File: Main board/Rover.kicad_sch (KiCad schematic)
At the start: 11 parts, among them J1 IN, J2 OUT, J3 Barrel_Jack_Switch, J4 MOTOR, J5 MOTOR, J6 MOTOR, J7 MOTOR, SW1 SW_DPDT_x2, U1 RASPBERRY_PI_4B_4GB

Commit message: updated pcb
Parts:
- removed U1: RASPBERRY_PI_4B_4GB, RASPBERRY_PI_4B_4GB:MODULE_RASPBERRY_PI_4B_4GB, symbol RASPBERRY_PI_4B_4GB:RASPBERRY_PI_4B_4GB
- added D1: LED, LED_THT:LED_D5.0mm_Clear, symbol Device:LED
- added J8: IMU, Connector_PinHeader_2.54mm:PinHeader_1x08_P2.54mm_Vertical, symbol Connector:Conn_01x04_Pin
- added U1: ESP32-DEVKITC-32D, Library:MODULE_ESP32-DEVKITC-32D, symbol ESP32-DEVKITC-32D:ESP32-DEVKITC-32D
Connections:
- net +5V: now also J8.1 (Pin_1), U1.J2-19 (EXT_5V)
- net GND: now also D1.1 (K), J8.2 (Pin_2), U1.J3-1 (GND3)
- net SIG A 1: now also U1.J2-6 (IO35)
- net SIG A 2: now also U1.J2-4 (SENSOR_VN)
- net SIG A 3: now also U1.J3-5 (RXD0)
- net SIG A 4: now also U1.J3-15 (IO2)
- net SIG B 1: now also U1.J2-5 (IO34)
- net SIG B 2: now also U1.J2-3 (SENSOR_VP)
- net SIG B 3: now also U1.J3-4 (TXD0)
- net SIG B 4: now also U1.J3-14 (IO0)
- net IN1 1: no longer names the net of U2.2 (IN1)
- net IN1 1: now also U1.J2-8 (IO33)
- net IN1 2: no longer names the net of U3.2 (IN1)
- net IN1 2: now also U1.J3-9 (IO18)
- net IN2 1: no longer names the net of U2.3 (IN2)
- net IN2 1: now also U1.J2-9 (IO25)
- net IN2 2: no longer names the net of U3.3 (IN2)
- net IN2 2: now also U1.J3-10 (IO5)
- net IN3 1: no longer names the net of U2.4 (IN3)
- net IN3 1: now also U1.J2-10 (IO26)
- net IN3 2: no longer names the net of U3.4 (IN3)
- net IN3 2: now also U1.J3-11 (IO17)
- net IN4 1: no longer names the net of U2.5 (IN4)
- net IN4 1: now also U1.J2-11 (IO27)
- net IN4 2: no longer names the net of U3.5 (IN4)
- net IN4 2: now also U1.J3-12 (IO16)
- net PWM0: no longer names the net of U3.1 (ENA)
- net PWM0: now also U1.J3-8 (IO19)
- net PWM1: no longer names the net of U2.1 (ENA)
- net PWM1: now also U1.J2-7 (IO32)
- net PWM2: no longer names the net of U3.6 (ENB)
- net PWM2: now also U1.J3-13 (IO4)
- net PWM3: no longer names the net of U2.6 (ENB)
- net PWM3: now also U1.J2-12 (IO14)
- new net: J8.3 (Pin_3), U1.J3-3 (IO22)
- new net: J8.4 (Pin_4), U1.J3-6 (IO21)
- new net: D1.2 (A), U1.J3-16 (IO15)
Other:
- note added: "6V MOTOR GND ENCODER GND ENCODER VCC SIG A SIG B"
- moved on the sheet: J1, J2, J3, J4, J5, J6, J7, SW1A, U2, U3

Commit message: message
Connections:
- net at J8.3 (Pin_3): no longer U1.J3-3 (IO22)
- net at J8.4 (Pin_4): no longer U1.J3-6 (IO21)
- net MOTOR_4_DIR_FORWARD: now reaches U2.4 (IN3)
- net MOTOR_4_DIR_FORWARD: now also U1.J3-13 (IO4); no longer U1.J2-10 (IO26)
- net MOTOR_1_DIR_FORWARD: now reaches U1.J2-11 (IO27)
- net MOTOR_1_DIR_FORWARD: now also U3.2 (IN1); no longer U2.5 (IN4)
- net MOTOR_1_DIR_REVERSE: now reaches U1.J2-12 (IO14)
- net MOTOR_1_DIR_REVERSE: now also U3.3 (IN2); no longer U2.6 (ENB)
- net MOTOR_2_DIR_FORWARD: now reaches U1.J2-13 (IO12)
- net MOTOR_2_DIR_FORWARD: now also U3.4 (IN3)
- net MOTOR_2_DIR_REVERSE: now reaches U1.J2-15 (IO13)
- net MOTOR_2_DIR_REVERSE: now also U3.5 (IN4)
- net MOTOR_1_PWM: now reaches U1.J2-7 (IO32)
- net MOTOR_1_PWM: now also U3.1 (ENA); no longer U2.1 (ENA)
- net MOTOR_2_PWM: now reaches U1.J2-8 (IO33)
- net MOTOR_2_PWM: now also U3.6 (ENB); no longer U2.2 (IN1)
- net MOTOR_3_DIR_REVERSE: now reaches U2.3 (IN2)
- net MOTOR_3_DIR_REVERSE: now also U1.J3-12 (IO16); no longer U1.J2-9 (IO25)
- net MOTOR_4_ENCODER_B: now reaches U1.J3-10 (IO5)
- net MOTOR_4_ENCODER_B: now also J5.6 (Pin_6); no longer U3.3 (IN2)
- net MOTOR_3_DIR_FORWARD: now reaches U1.J3-11 (IO17)
- net MOTOR_3_DIR_FORWARD: now also U2.2 (IN1); no longer U3.4 (IN3)
- net MOTOR_1_ENCODER_A: now reaches U1.J3-2 (IO23)
- net MOTOR_1_ENCODER_A: now also J6.5 (Pin_5)
- net MOTOR_3_ENCODER_B: now reaches U1.J3-8 (IO19)
- net MOTOR_3_ENCODER_B: now also J4.6 (Pin_6); no longer U3.1 (ENA)
- net MOTOR_4_ENCODER_A: now reaches U1.J3-9 (IO18)
- net MOTOR_4_ENCODER_A: now also J5.5 (Pin_5); no longer U3.2 (IN1)
- net SIG A 1: no longer names the net of U1.J2-6 (IO35)
- net SIG A 1: no longer J4.5 (Pin_5)
- net SIG A 2 renamed MOTOR_2_ENCODER_B
- net MOTOR_2_ENCODER_B: now also J7.6 (Pin_6); no longer J5.5 (Pin_5)
- net SIG A 3: no longer names the net of U1.J3-5 (RXD0)
- net SIG A 3: no longer J6.5 (Pin_5)
- net SIG A 4: no longer names the net of U1.J3-15 (IO2)
- net SIG A 4: no longer J7.5 (Pin_5)
- net SIG B 1: no longer names the net of U1.J2-5 (IO34)
- net SIG B 1: no longer J4.6 (Pin_6)
- net SIG B 2 renamed MOTOR_2_ENCODER_A
- net MOTOR_2_ENCODER_A: now also J7.5 (Pin_5); no longer J5.6 (Pin_6)
- net SIG B 3: no longer names the net of U1.J3-4 (TXD0)
- net SIG B 3: no longer J6.6 (Pin_6)
- net SIG B 4 renamed MOTOR_4_DIR_REVERSE
- net MOTOR_4_DIR_REVERSE: now also U2.5 (IN4); no longer J7.6 (Pin_6)
- new net MOTOR_1_ENCODER_B: J6.6 (Pin_6), U1.J3-3 (IO22)
- new net MOTOR_3_ENCODER_A: J4.5 (Pin_5), U1.J3-6 (IO21)
- new net MOTOR_3_PWM: U1.J2-9 (IO25), U2.1 (ENA)
- new net MOTOR_4_PWM: U1.J2-10 (IO26), U2.6 (ENB)
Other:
- moved on the sheet: D1, J1, J2, J3, J4, J5, J6, J7, J8, SW1A, U1, U3

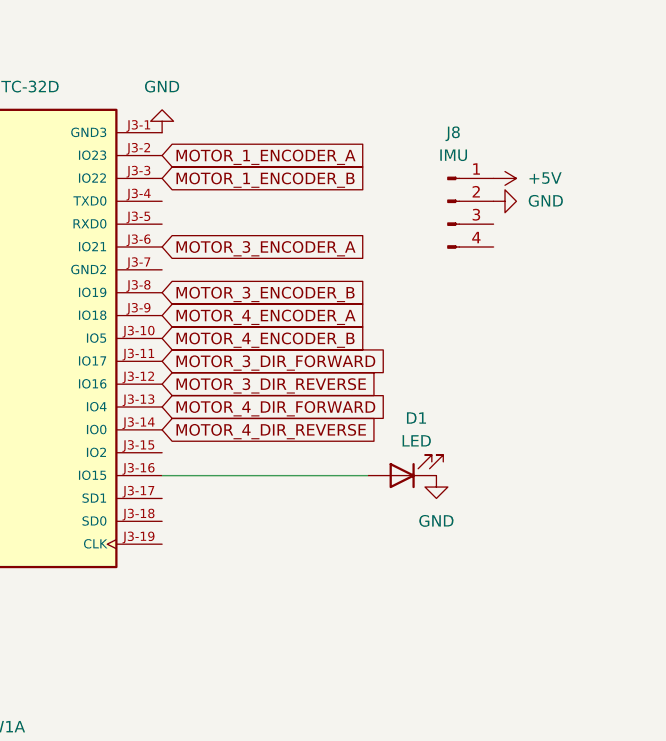
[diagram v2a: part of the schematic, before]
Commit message: add edge detection
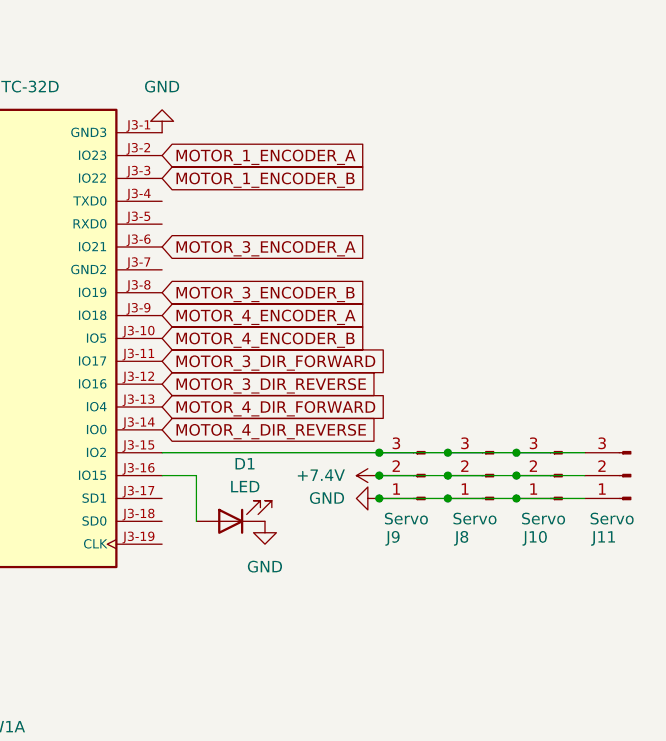
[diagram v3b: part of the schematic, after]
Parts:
- removed J8: IMU, Connector_PinHeader_2.54mm:PinHeader_1x08_P2.54mm_Vertical, symbol Connector:Conn_01x04_Pin
- added J10, J11, J8, J9: Servo, Connector_PinHeader_2.54mm:PinHeader_1x03_P2.54mm_Vertical, symbol Connector:Conn_01x03_Pin
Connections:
- net +7.4V: now also J10.2 (Pin_2), J11.2 (Pin_2), J8.2 (Pin_2), J9.2 (Pin_2)
- net GND: now also J10.1 (Pin_1), J11.1 (Pin_1), J8.1 (Pin_1), J9.1 (Pin_1)
- net at U1.J3-15 (IO2): now also J10.3 (Pin_3), J11.3 (Pin_3), J8.3 (Pin_3), J9.3 (Pin_3)
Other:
- moved on the sheet: D1
